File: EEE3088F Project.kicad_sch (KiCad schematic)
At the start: 54 parts, among them J1 Conn_02x16_Odd_Even, J2 Battery IN JST, M1Control1 DRV8837, M2Control1 DRV8837, M3Control1 DRV8837, M4Control1 DRV8837, Q1 AO3400A, U1 TP4056-42-ESOP8, U2 TPS62163DSG, U3 CH224K, U4 TPS62162DSG, U5 MT3608

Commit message: Cleaned up battery charging circuit and added Battery, 3V3_out and 5V_out labels to motherboard connection
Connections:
- net 3V3 is gone; now on net 3V3_out: C15.1, L2.2, R7.2, U4.6 (VOS)
- net 5V is gone; now on net 5V_out: C14.1, C17.1, D1.1 (K), R9.1, U4.2 (VIN), U4.3 (EN)
- net GND: now also USB1.1 (SHELL), USB1.2 (SHELL), USB1.3 (SHELL), USB1.4 (SHELL)
- net VBatt: now also J1.14 (Pin_14)
- net 3V3_out: now reaches J1.18 (Pin_18)
- net 5V_out: now reaches J1.20 (Pin_20)
- net CC2: now reaches U3.6 (CC2), USB1.B5 (CC2)
- net CC1: now reaches U3.7 (CC1), USB1.A5 (CC1)
- net VBUS_USBC: now reaches R5.1, USB1.A4B9 (VBUS), USB1.B4A9 (VBUS)
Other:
- moved on the sheet: J1, R5, R6

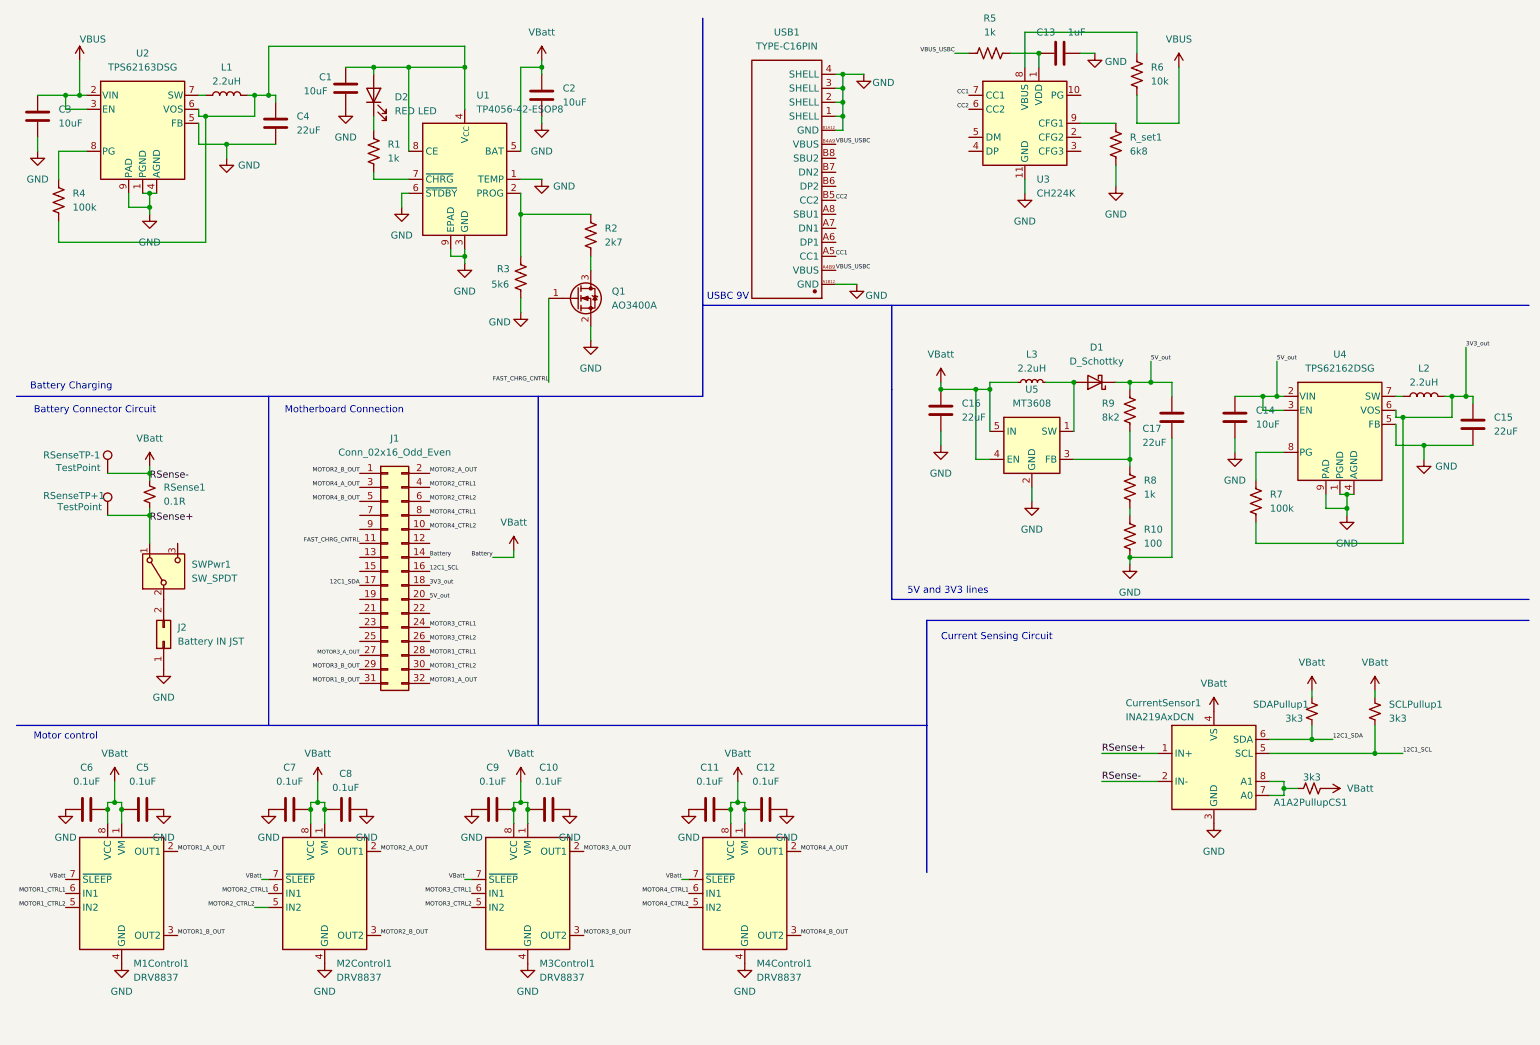
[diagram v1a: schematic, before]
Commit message: Added external load switching circuit
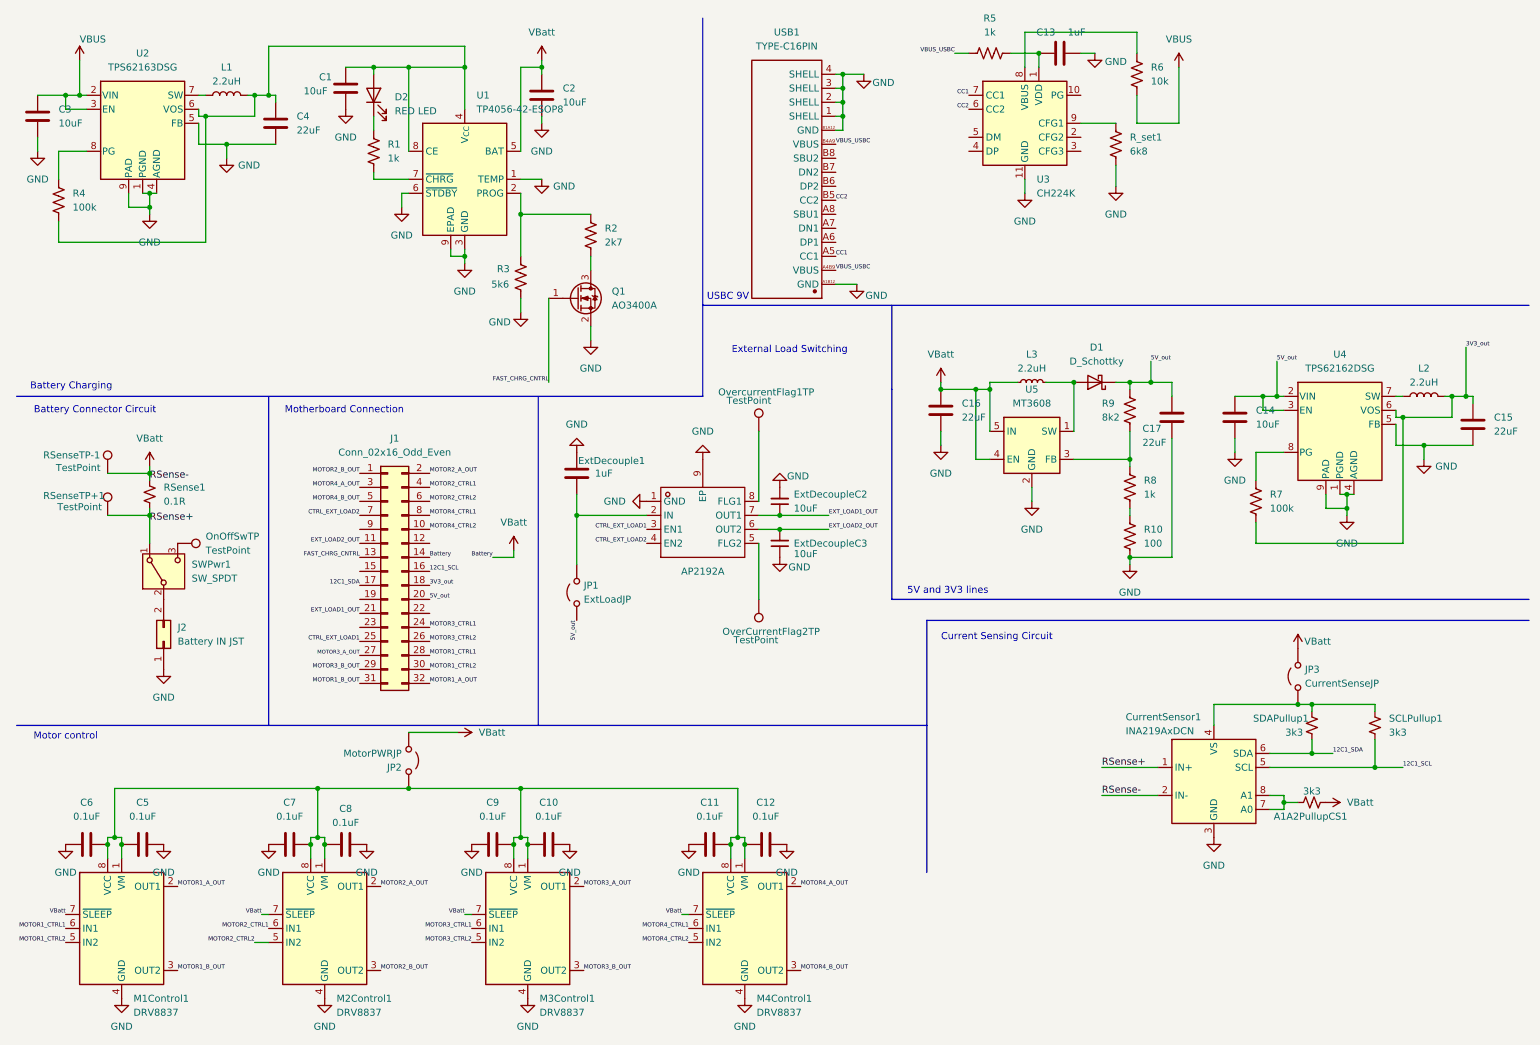
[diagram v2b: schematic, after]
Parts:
- added AP2192A: ~, Custom Footprints:MSOP-8_L3.0-W3.0-P0.65-LS4.9-BL-EP1.8, symbol Custom Symbols:AP2192AMPG-13
- added ExtDecouple1: 1uF, Capacitor_SMD:C_0603_1608Metric_Pad1.08x0.95mm_HandSolder, symbol Device:C
- added ExtDecoupleC2, ExtDecoupleC3: 10uF, Capacitor_SMD:C_0805_2012Metric_Pad1.18x1.45mm_HandSolder, symbol Device:C_Small
- added JP1: ExtLoadJP, symbol Jumper:Jumper_2_Open
- added JP2: MotorPWRJP, symbol Jumper:Jumper_2_Open
- added JP3: CurrentSenseJP, symbol Jumper:Jumper_2_Open
- added OnOffSwTP, OverCurrentFlag2TP, OvercurrentFlag1TP: TestPoint, symbol Connector:TestPoint
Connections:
- net 5V_out: now also JP1.1 (A)
- net FAST_CHRG_CNTRL: now also J1.13 (Pin_13); no longer J1.11 (Pin_11)
- net GND: now also AP2192A.1 (GND), AP2192A.9 (EP), ExtDecouple1.2, ExtDecoupleC2.2, ExtDecoupleC3.1
- net VBatt: now also JP2.1 (A), JP3.2 (B); no longer C10.1, C11.2, C12.1, C5.1, C6.2, C7.2, C8.1, C9.2, CurrentSensor1.4 (VS), M1Control1.1 (VM), M1Control1.8 (VCC), M2Control1.1 (VM), M2Control1.8 (VCC), M3Control1.1 (VM), M3Control1.8 (VCC), M4Control1.1 (VM), M4Control1.8 (VCC), SCLPullup1.1, SDAPullup1.1
- net EXT_LOAD1_OUT: now reaches J1.21 (Pin_21)
- net EXT_LOAD1_OUT: now also AP2192A.7 (OUT1), ExtDecoupleC2.1
- net CTRL_EXT_LOAD1: now reaches J1.25 (Pin_25)
- net CTRL_EXT_LOAD1: now also AP2192A.3 (EN1)
- net CTRL_EXT_LOAD2: now reaches J1.7 (Pin_7)
- net CTRL_EXT_LOAD2: now also AP2192A.4 (EN2)
- net at SWPwr1.3 (C): now also OnOffSwTP.1
- new net: CurrentSensor1.4 (VS), JP3.1 (A), SCLPullup1.1, SDAPullup1.1
- new net: C10.1, C11.2, C12.1, C5.1, C6.2, C7.2, C8.1, C9.2, JP2.2 (B), M1Control1.1 (VM), M1Control1.8 (VCC), M2Control1.1 (VM), M2Control1.8 (VCC), M3Control1.1 (VM), M3Control1.8 (VCC), M4Control1.1 (VM), M4Control1.8 (VCC)
- new net: AP2192A.2 (IN), ExtDecouple1.1, JP1.2 (B)
- new net: AP2192A.8 (FLG1), OvercurrentFlag1TP.1
- new net: AP2192A.5 (FLG2), OverCurrentFlag2TP.1
- new net EXT_LOAD2_OUT: AP2192A.6 (OUT2), ExtDecoupleC3.2, J1.11 (Pin_11)
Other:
- note added: "External Load Switching"
- moved on the sheet: A1A2PullupCS1, C10, C11, C12, C5, C6, C7, C8, C9, CurrentSensor1, M1Control1, M2Control1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
